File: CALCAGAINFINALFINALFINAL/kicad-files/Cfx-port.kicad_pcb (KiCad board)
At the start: 4 copper layers, 65 x 140 mm, 76 parts, among them J2 USB_C_Receptacle_USB2.0_16P, J3 Micro_SD_Card, J4 Conn_01x02, SW100 SW_SPST, SW101 SW_SPST, SW102 SW_SPST, SW49 SW_SPST, SW52 SW_SPST, SW55 SW_SPST, SW56 SW_SPST, SW57 SW_SPST, SW58 SW_SPST, SW59 SW_SPST, SW60 SW_SPST, SW61 SW_SPST, SW62 SW_SPST, SW63 SW_SPST, SW64 SW_SPST, SW65 SW_SPST, SW66 SW_SPST, SW67 SW_SPST, SW68 SW_SPST, SW69 SW_SPST, SW70 SW_SPST, SW71 SW_SPST, SW72 SW_SPST, SW73 SW_SPST, SW74 SW_SPST, SW75 SW_SPST, SW76 SW_SPST, SW77 SW_SPST, SW78 SW_SPST, SW79 SW_SPST, SW80 SW_SPST, SW81 SW_SPST, SW82 SW_SPST, SW83 SW_SPST, SW84 SW_SPST, SW85 SW_SPST, SW86 SW_SPST, SW87 SW_SPST, SW88 SW_SPST, SW89 SW_SPST, SW90 SW_SPST, SW91 SW_SPST, SW92 SW_SPST, SW93 SW_SPST, SW94 SW_SPST, SW95 SW_SPST, SW96 SW_SPST, SW97 SW_SPST, SW98 SW_SPST, SW99 SW_SPST, U5 TP4056-42-ESOP8, U6 TLV61070ADBV, U7 TCA9535DBR

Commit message: I reckon its all done now. need to doucble check all pin assignments tomorrow and then add camera then order everything. we might lowkirkenuinely launch this shit chat
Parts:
- removed the REF** at (156.1, 37.4)
- removed REF1: ESP32-S3R8, ButtonPads:QFN40P700X700X90-57N
- added C1: 0.1, Capacitor_SMD:C_0603_1608Metric, B.Cu at (150.3, 57.1)
- added R8: 5.1k, Resistor_SMD:R_0201_0603Metric, B.Cu at (152.8, 84.7)
- added R8: 5.1k, Resistor_SMD:R_0201_0603Metric, B.Cu at (152.8, 83.6)
- added REF**: 10k, Resistor_SMD:R_01005_0402Metric, B.Cu at (137.2, 32.0)
- added REF**: SW_SPST_B3U-1000P, Button_Switch_SMD:SW_SPST_B3U-1000P, B.Cu at (149.9, 62.2)
- added REF**: SW_SPST_B3U-1000P, Button_Switch_SMD:SW_SPST_B3U-1000P, B.Cu at (137.3, 28.6)
- added REF**: 10k, Resistor_SMD:R_01005_0402Metric, B.Cu at (151.4, 54.7)
- added U8: ESP32-S3-WROOM-1, RF_Module:ESP32-S3-WROOM-1, B.Cu at (148.3, 42.6)
- C1: value C -> 0.1; footprint Capacitor_SMD:C_1812_4532Metric -> Capacitor_SMD:C_0603_1608Metric
- C2: value C -> 10uf; footprint Capacitor_SMD:C_1812_4532Metric -> Capacitor_SMD:C_0603_1608Metric
- C4, C5, C6: footprint Capacitor_SMD:C_1812_4532Metric -> Capacitor_SMD:C_0603_1608Metric
- L2: footprint Capacitor_SMD:C_1812_4532Metric -> Inductor_SMD:L_6.3x6.3_H3
- R8: value 5.1kΩ -> 5.1k
- R9: value R -> 5.1k
- moved U7 58.7 mm to (131.0, 62.9)
- moved J2 58.0 mm to (158.8, 84.5), turned to -90 degrees
- moved C1 50.9 mm to (112.6, 33.0), turned to 90 degrees
- moved R2 50.2 mm to (130.5, 30.3), turned to 90 degrees
- moved J3 48.7 mm to (122.5, 34.0), turned to 90 degrees
- moved R8 45.9 mm to (152.8, 82.7), turned to 180 degrees
- moved R9 44.2 mm to (152.8, 85.7), turned to 180 degrees
- moved C2 43.2 mm to (114.2, 33.0), turned to 90 degrees
- moved R1 41.9 mm to (130.6, 34.6), turned to 90 degrees
- moved J4 41.4 mm to (144.2, 106.2), turned to 180 degrees
- moved R3 38.6 mm to (130.6, 36.5), turned to -90 degrees
- moved L2 37.4 mm to (137.6, 95.1), turned to -90 degrees
- moved U6 33.4 mm to (135.2, 103.0), turned to 180 degrees
- moved D15 33.4 mm to (145.6, 87.3), turned to 180 degrees
- moved R11 30.6 mm to (144.1, 86.2), turned to 180 degrees
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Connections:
- net D+ renamed Net-(J2-D+-PadA6)
- net D- renamed Net-(J2-D--PadA7)
- C1 pad 1: VCC -> 3V3
- C2 pad 1: VCC -> 3V3
- C4 pad 2: /power-ic/VBAT_SW -> /power-ic/BAT+
- C6 pad 2: VCC -> 3V3
- J3 pad 2: /esp32-s3 pinout/CS -> /esp32-s3 pinout/CS1
- J3 pad 4: VCC -> 3V3
- L2 pad 1: /power-ic/VBAT_SW -> /power-ic/BAT+
- R1 pad 2: VCC -> 3V3
- R11 pad 1: VCC -> Net-(D20-A)
- R14 pad 1: VCC -> 3V3
- R2 pad 2: VCC -> 3V3
- R3 pad 1: /esp32-s3 pinout/CS -> /esp32-s3 pinout/CS1
- R3 pad 2: VCC -> 3V3
- U5 pad 4: /power-ic/VBAT_SW -> /power-ic/BAT+
- U6 pad 3: /power-ic/VBAT_SW -> /power-ic/BAT+
- U6 pad 5: VCC -> 3V3
- U6 pad 6: /power-ic/VBAT_SW -> /power-ic/BAT+
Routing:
- net 3V3: track 0.00 -> 189.7 mm, vias 0 -> 6
- net /Keypad Matrix/R5: track 0.00 -> 158.3 mm, vias 0 -> 7
- net /Keypad Matrix/R6: track 6.63 -> 155.0 mm, vias 1 -> 6
- net /Keypad Matrix/R9: track 40.2 -> 181.8 mm, vias 1 -> 6
- net /Keypad Matrix/C4: track 26.7 -> 148.1 mm, vias 0 -> 1
- net /Keypad Matrix/R4: track 16.3 -> 133.4 mm, vias 0 -> 7
- net /Keypad Matrix/C3: track 37.1 -> 143.1 mm, vias 0 -> 1
- net /Keypad Matrix/C1: track 56.1 -> 156.2 mm, vias 0 -> 1
- net /Keypad Matrix/C2: track 47.4 -> 144.5 mm, vias 0 -> 1
- net /Keypad Matrix/R1: track 27.8 -> 123.9 mm, vias 1 -> 6
- net /Keypad Matrix/R7: track 67.6 -> 162.5 mm, vias 5 -> 6
- net /Keypad Matrix/R8: track 85.9 -> 175.0 mm, vias 5 -> 6
- net /Keypad Matrix/C6: track 8.69 -> 97.8 mm, vias 0 -> 1
- net /esp32-s3 pinout/SCK: track 0.00 -> 60.5 mm, vias 0 -> 2
- net /Keypad Matrix/R3: track 82.7 -> 139.0 mm, vias 4 -> 7
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- added copper zone on In1.Cu, net GND
- removed copper zone on In2.Cu, net GND
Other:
- board size 65 x 140 mm -> 65 x 135.9 mm
- board text added: "BOOT"
- board text added: "RESET"
- board text removed: "1.fix diode removal 2.add camera connector finalise pinout"
- board text removed: "3000mah bat"

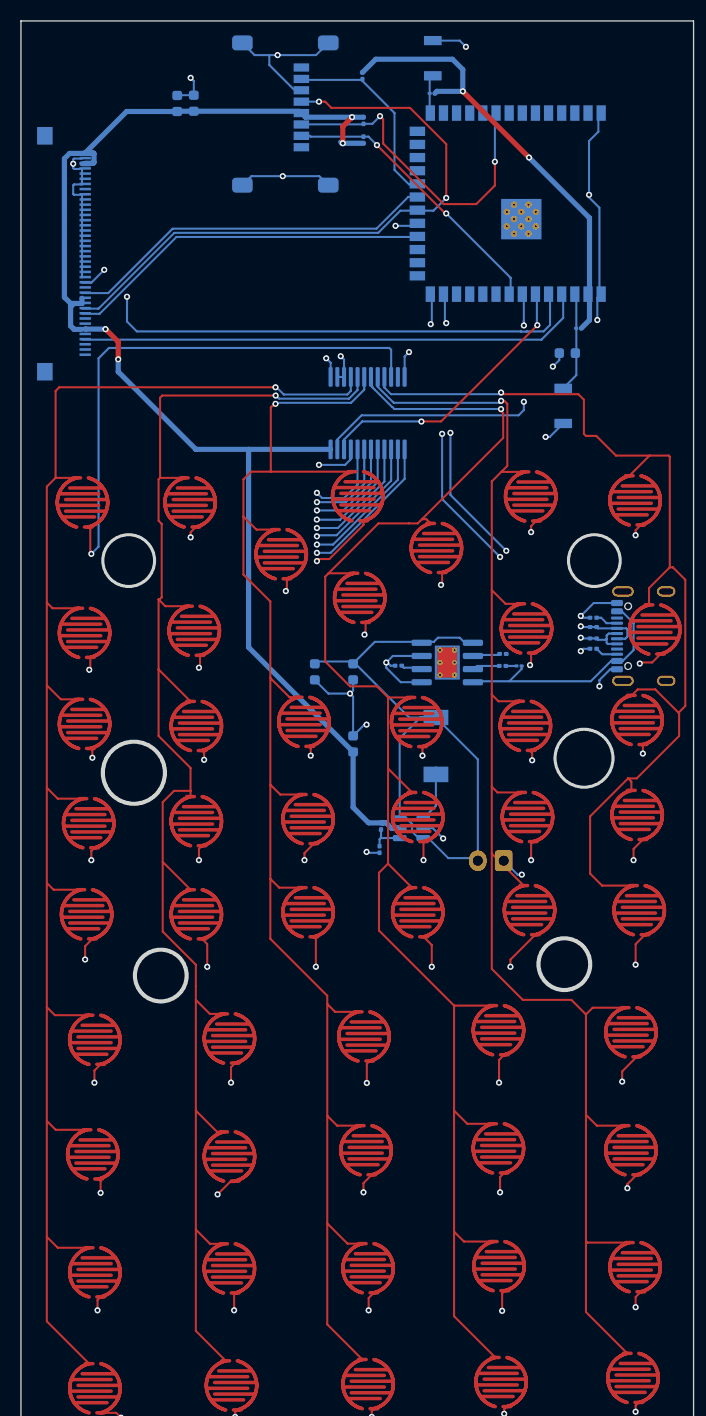
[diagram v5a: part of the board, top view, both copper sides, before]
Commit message: finished pcb up until no camera connector. gona add camera and then order pcba and screen and shi
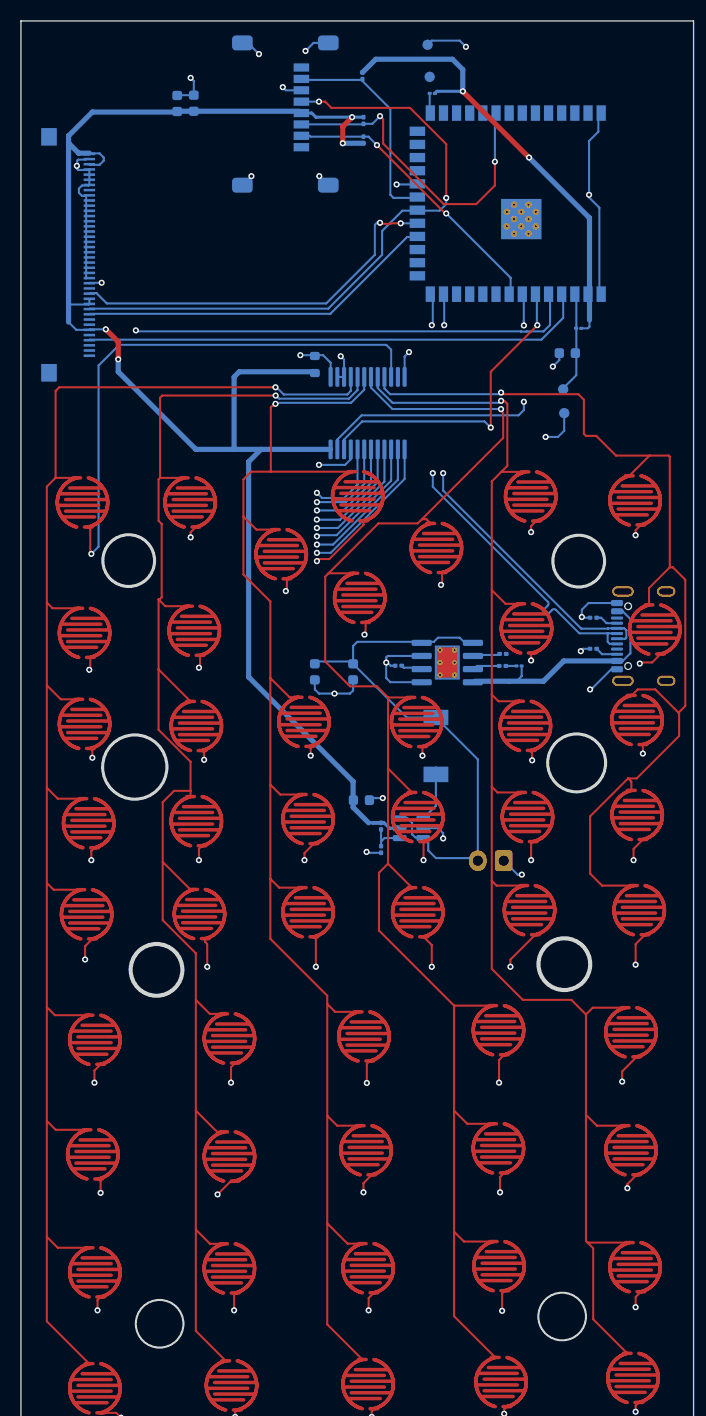
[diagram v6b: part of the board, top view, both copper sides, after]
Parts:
- removed the R8 at (152.8, 84.7)
- removed the R8 at (152.8, 83.6)
- removed the REF** at (149.9, 62.2)
- removed the REF** at (137.3, 28.6)
- added REF**: TestPoint_Pad_D1.0mm, TestPoint:TestPoint_Pad_D1.0mm, B.Cu at (150.0, 62.9)
- added REF**: TestPoint_Pad_D1.0mm, TestPoint:TestPoint_Pad_D1.0mm, B.Cu at (137.0, 30.4)
- added REF**: R_0603_1608Metric, Resistor_SMD:R_0603_1608Metric, B.Cu at (125.9, 58.2)
- added REF**: TestPoint_Pad_D1.0mm, TestPoint:TestPoint_Pad_D1.0mm, B.Cu at (136.8, 27.3)
- added REF**: TestPoint_Pad_D1.0mm, TestPoint:TestPoint_Pad_D1.0mm, B.Cu at (149.9, 60.6)
- R12: value R -> 1.2
- R2: value R -> 10k
- moved C6 5.50 mm to (130.4, 100.3), turned to 180 degrees
- moved REF** 0.41 mm to (102.1, 47.6)
- moved SW66 0.30 mm to (114.7, 111.3)
- moved R13 0.14 mm to (132.3, 105.1)
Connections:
- net Net-(J2-D+-PadA6) renamed usb_P
- net Net-(J2-D--PadA7) renamed usb_N
- U8 pad 19: ~{INT} -> /esp32-s3 pinout/MOSI
- U8 pad 21: /esp32-s3 pinout/MOSI -> /esp32-s3 pinout/MISO
- U8 pad 22: /esp32-s3 pinout/MISO -> ~{INT}
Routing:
- net 3V3: track 189.7 -> 209.6 mm
- net GND: track 113.7 -> 96.4 mm, vias 21 -> 23
- net /power-ic/BAT+: track 63.0 -> 52.3 mm
- net ~{INT}: track 19.9 -> 29.5 mm
- net SCL: track 27.2 -> 30.8 mm
- net /Keypad Matrix/R8: track 175.0 -> 178.7 mm
- net /esp32-s3 pinout/RST: track 53.1 -> 50.5 mm
- net /esp32-s3 pinout/MISO: track 18.9 -> 20.8 mm
- net boot: track 3.15 -> 1.75 mm
- net /Keypad Matrix/R4: track 133.4 -> 134.7 mm
- net /Keypad Matrix/R5: track 158.3 -> 157.1 mm
- net VCC: track 22.8 -> 23.9 mm
- net /Keypad Matrix/C5: track 143.5 -> 142.5 mm
- net /esp32-s3 pinout/SCK: track 60.5 -> 61.5 mm
- net /Keypad Matrix/C4: track 148.1 -> 149.0 mm
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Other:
- outline, holes or cut-outs redrawn

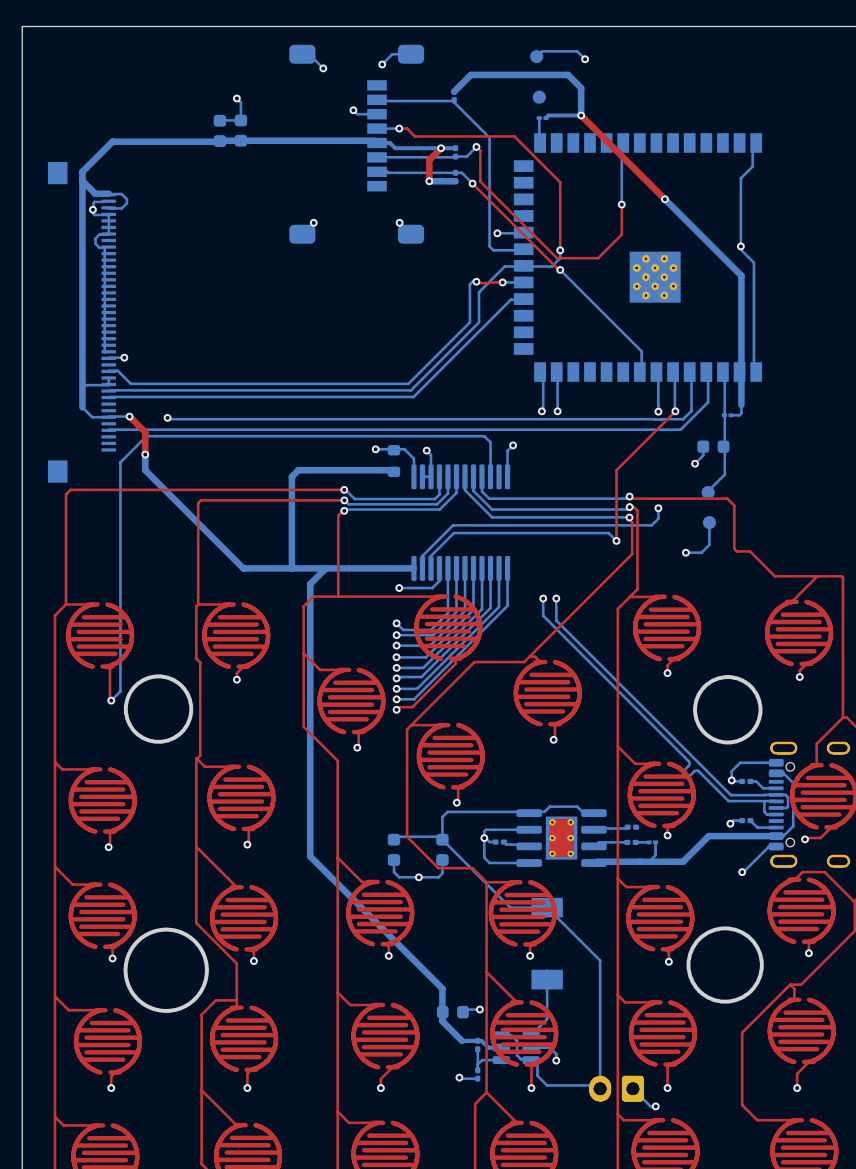
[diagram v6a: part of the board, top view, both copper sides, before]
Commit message: finalised pcb w camera. thing is im kinda poor rn and ill prob get enough money to order pcba after 2 weeks. until then ima js focus on school and get thru to working on tweaking the HAL and ui to match my spec and the design language of ABSOLUT-CAS
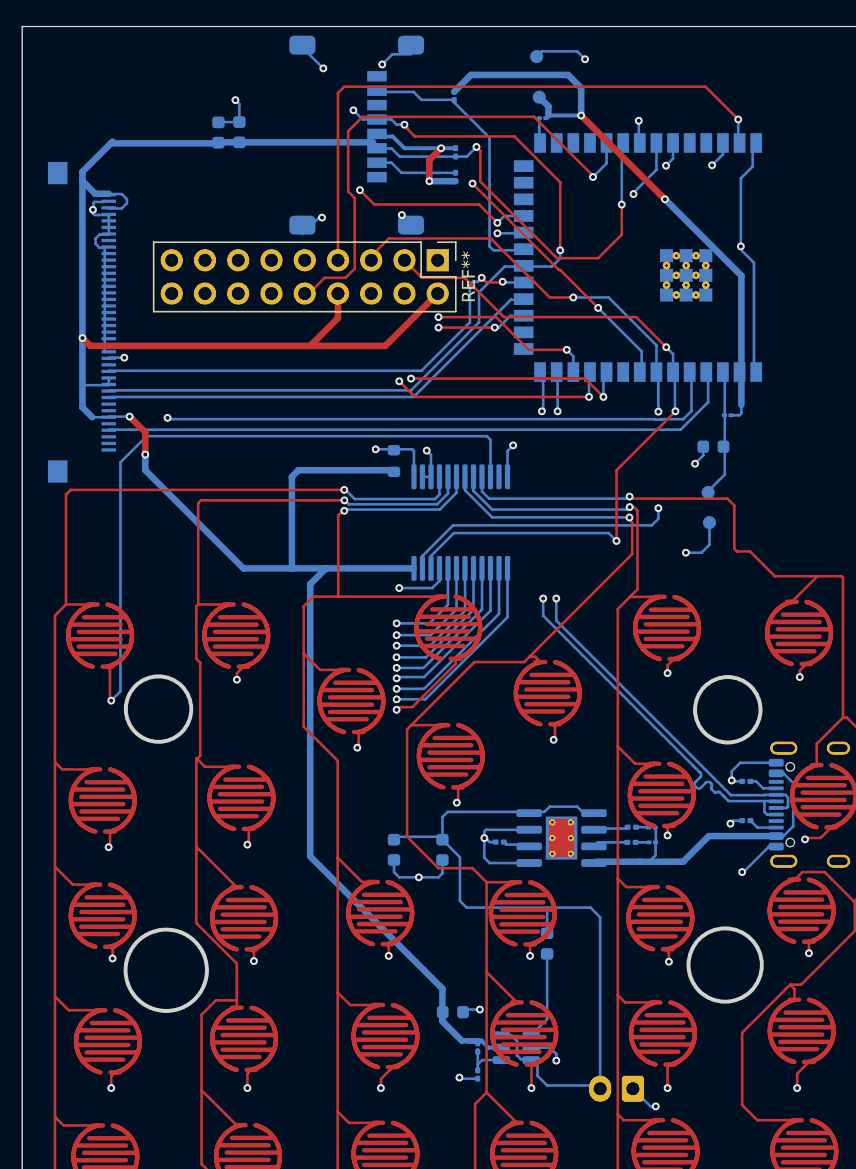
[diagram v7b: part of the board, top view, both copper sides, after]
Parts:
- added D15: LED, LED_SMD:LED_01005_0402Metric, B.Cu at (145.6, 86.2)
- added REF**: PinHeader_2x09_P2.54mm_Vertical, Connector_PinHeader_2.54mm:PinHeader_2x09_P2.54mm_Vertical, F.Cu at (129.2, 42.9)
- L2: footprint Inductor_SMD:L_6.3x6.3_H3 -> Inductor_SMD:L_0603_1608Metric
- U8: value ESP32-S3-WROOM-1 -> ESP32-S3-WROOM-2; footprint RF_Module:ESP32-S3-WROOM-1 -> RF_Module:ESP32-S3-WROOM-2
- moved J3 0.70 mm to (122.5, 33.3)
- moved R14 0.19 mm to (132.3, 103.0)
- moved C1 0.17 mm to (112.5, 33.1)
- moved C2 0.17 mm to (114.1, 33.1)
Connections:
- REF** pad 1: (no net) -> 3V3
- U8 pad 10: unconnected-(U8-IO17-Pad10) -> OV_D5
- U8 pad 11: unconnected-(U8-IO18-Pad11) -> OV_D6
- U8 pad 12: /esp32-s3 pinout/extra -> OV_D3
- U8 pad 15: unconnected-(U8-IO3-Pad15) -> (no net)
- U8 pad 17: unconnected-(U8-IO9-Pad17) -> OV_D4
- U8 pad 23: unconnected-(U8-IO21-Pad23) -> OV_D7
- U8 pad 31: unconnected-(U8-IO38-Pad31) -> OV_D2
- U8 pad 33: unconnected-(U8-IO40-Pad33) -> OV_PCLK
- U8 pad 34: unconnected-(U8-IO41-Pad34) -> OV_VSYNC
- U8 pad 35: unconnected-(U8-IO42-Pad35) -> OV_HREF
- U8 pad 38: unconnected-(U8-IO2-Pad38) -> OV_D1
- U8 pad 39: unconnected-(U8-IO1-Pad39) -> OV_D0
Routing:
- net OV_D0: track 0.00 -> 46.3 mm, vias 0 -> 1
- net OV_PCLK: track 0.00 -> 44.6 mm, vias 0 -> 1
- net OV_D2: track 0.00 -> 39.5 mm, vias 0 -> 1
- net OV_D1: track 0.00 -> 38.1 mm, vias 0 -> 1
- net OV_D5: track 0.00 -> 36.5 mm, vias 0 -> 2
- net 3V3: track 209.6 -> 245.5 mm, vias 6 -> 7
- net OV_D6: track 0.00 -> 35.2 mm, vias 0 -> 2
- net OV_HREF: track 0.00 -> 33.0 mm, vias 0 -> 1
- net OV_D7: track 0.00 -> 31.8 mm, vias 0 -> 2
- net OV_D3: track 0.00 -> 28.8 mm, vias 0 -> 2
- net SDA: track 31.3 -> 59.1 mm, vias 2 -> 3
- net OV_VSYNC: track 0.00 -> 27.7 mm, vias 0 -> 1
- net SCL: track 30.8 -> 55.7 mm, vias 2 -> 3
- net OV_D4: track 0.00 -> 21.9 mm, vias 0 -> 2
- net /power-ic/BAT+: track 52.3 -> 58.2 mm
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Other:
- board text added: "gnd"

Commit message: hgjfhgjfhgfjghfjghf
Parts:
- removed the REF** at (150.0, 62.9)
- removed the REF** at (137.0, 30.4)
- removed the REF** at (136.8, 27.3)
- removed the REF** at (149.9, 60.6)
- added ?: 10k, Resistor_SMD:R_0201_0603Metric, B.Cu at (131.6, 84.9)
- added ?: 10k, Resistor_SMD:R_0201_0603Metric, B.Cu at (133.4, 84.9)
- added REF**: SW_Push_1P1T_NO_CK_KMR2, Button_Switch_SMD:SW_Push_1P1T_NO_CK_KMR2, B.Cu at (150.2, 62.5)
- added REF**: SW_Push_1P1T_NO_CK_KMR2, Button_Switch_SMD:SW_Push_1P1T_NO_CK_KMR2, B.Cu at (135.7, 28.6)
- moved REF** 8.63 mm to (134.5, 57.5), turned to 180 degrees
- moved U7 7.21 mm to (138.2, 63.2)
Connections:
- U8 pad 24: unconnected-(U8-IO47-Pad24) -> batprog
- U8 pad 35: OV_HREF -> (no net)
- U8 pad 9: /esp32-s3 pinout/~{INT1} -> OV_HREF
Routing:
- net batprog: track 0.00 -> 61.5 mm, vias 0 -> 3
- net /Keypad Matrix/R1: track 123.9 -> 95.5 mm, vias 6 -> 7
- net OV_HREF: track 33.0 -> 22.6 mm, vias 1 -> 2
- net /Keypad Matrix/C6: track 97.8 -> 89.4 mm
- net /Keypad Matrix/R3: track 139.4 -> 147.5 mm
- net /Keypad Matrix/R2: track 144.8 -> 153.0 mm
- net /Keypad Matrix/R4: track 134.8 -> 142.9 mm
- net /Keypad Matrix/R5: track 157.2 -> 165.2 mm
- net /Keypad Matrix/R6: track 155.0 -> 162.7 mm
- net /power-ic/BAT+: track 58.2 -> 65.7 mm
- net /Keypad Matrix/R7: track 162.5 -> 170.0 mm
- net /Keypad Matrix/C5: track 142.5 -> 135.2 mm
- net /Keypad Matrix/R8: track 178.6 -> 185.7 mm
- net SCL: track 55.7 -> 48.6 mm
- net GND: track 94.8 -> 101.9 mm
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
